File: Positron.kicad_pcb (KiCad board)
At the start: 4 copper layers, 66.5 x 88.5 mm, 114 parts, among them CN1 GT-3321667P-01, J1 USB_C_Receptacle_USB2.0_16P, J2 Conn_01x04_Socket, J3 AudioJack3_SwitchTR, J4 PJ-603, J5 PJ-603, Q1 DMG1012T, SW1 TS-1187A-B-A-B, SW2 TS-1187A-B-A-B, U1 CS43198-CNZ, U10 SSM2019BRNZ, U2 TPS7A2036DBV, U3 TPS7A2018DBV, U4 STM32H743VITx, U5 RT6150AGQW, U6 OPA4134, U7 LM2776DBVR, U8 CS5361, U9 SSM2019BRNZ, Y1 Crystal_GND24

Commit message: fix balanced mic input
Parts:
- removed R18, R20: 400R, Resistor_SMD:R_0402_1005Metric
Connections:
- J4 pad 4: unconnected-(J4-Pad4) -> Net-(U9--IN)
- J5 pad 4: unconnected-(J5-Pad4) -> Net-(U10--IN)
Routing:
- net Net-(U10--IN): track 2.34 -> 9.40 mm
- net Net-(U9--IN): track 2.84 -> 9.03 mm
- net GND: track 748.7 -> 748.6 mm, vias 67 -> 66

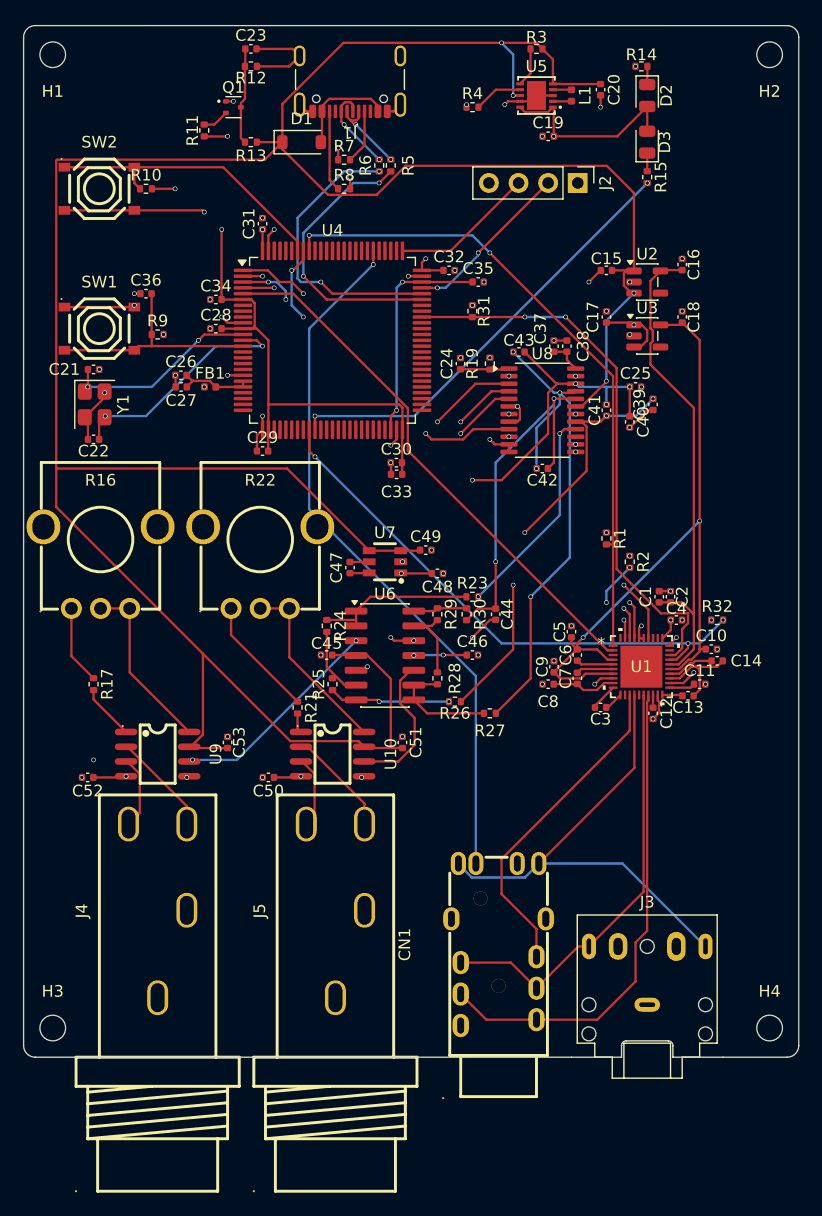
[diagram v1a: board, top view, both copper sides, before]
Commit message: separate GND planes and fill copper zone
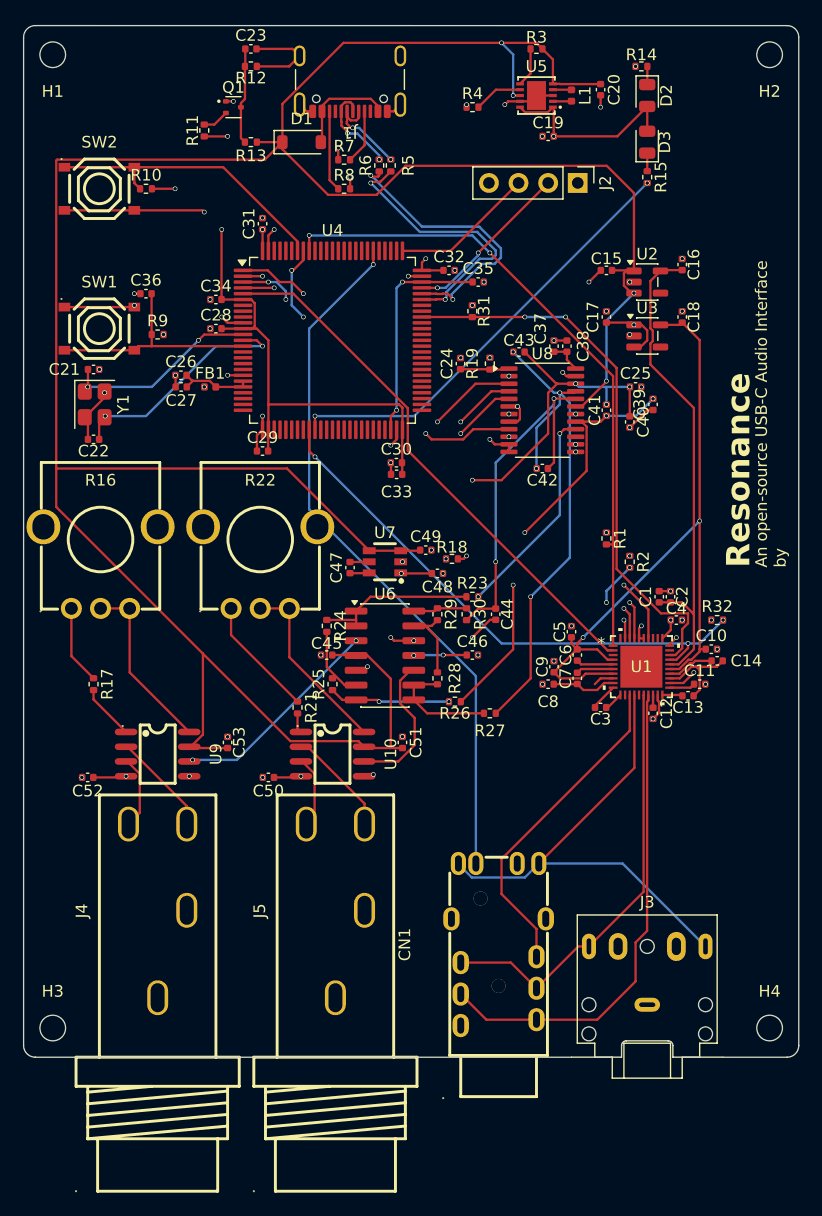
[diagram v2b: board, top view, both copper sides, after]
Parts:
- added R18: 0R, Resistor_SMD:R_0402_1005Metric, F.Cu at (48.8, 57.8)
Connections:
- C10 pad 2: GND -> GNDA
- C11 pad 2: GND -> GNDA
- C12 pad 2: GND -> GNDA
- C45 pad 2: GND -> GNDA
- C46 pad 2: GND -> GNDA
- C48 pad 1: GND -> GNDA
- C49 pad 2: GND -> GNDA
- C50 pad 2: GND -> GNDA
- C51 pad 1: GND -> GNDA
- C52 pad 2: GND -> GNDA
- C53 pad 1: GND -> GNDA
- C8 pad 1: GND -> GNDA
- C9 pad 1: GND -> GNDA
- CN1 pad 1: GND -> GNDA
- CN1 pad 11: GND -> GNDA
- CN1 pad 12: GND -> GNDA
- CN1 pad 9: GND -> GNDA
- J3 pad S: GND -> GNDA
- J4 pad 2: GND -> GNDA
- J5 pad 2: GND -> GNDA
- U1 pad 19: GND -> GNDA
- U1 pad 8: GND -> GNDA
- U10 pad 5: GND -> GNDA
- U7 pad 2: GND -> GNDA
- U9 pad 5: GND -> GNDA
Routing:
- net GND: track 748.6 -> 463.8 mm, vias 66 -> 49
- net GNDA: track 0.00 -> 206.1 mm, vias 0 -> 17
- net Net-(J1-D--PadA7): track 7.08 -> 8.37 mm
- added copper zone on In1.Cu, net GND
- added copper zone on In1.Cu, net GNDA
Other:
- board text added: "An open-source USB-C Audio Interface by"
- board text added: "Resonance"
